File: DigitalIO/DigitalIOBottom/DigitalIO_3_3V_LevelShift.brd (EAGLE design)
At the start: 64 x 82 mm, 72 parts, among them IC1 MCP23017SP, IC2 ULN2803A, K5 HF46105, K6 HF46105, K7 HF46105, K8 HF46105, P1 DF11-06-2DSA, Q1 BS170, Q2 BS170, Q5 691131710002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

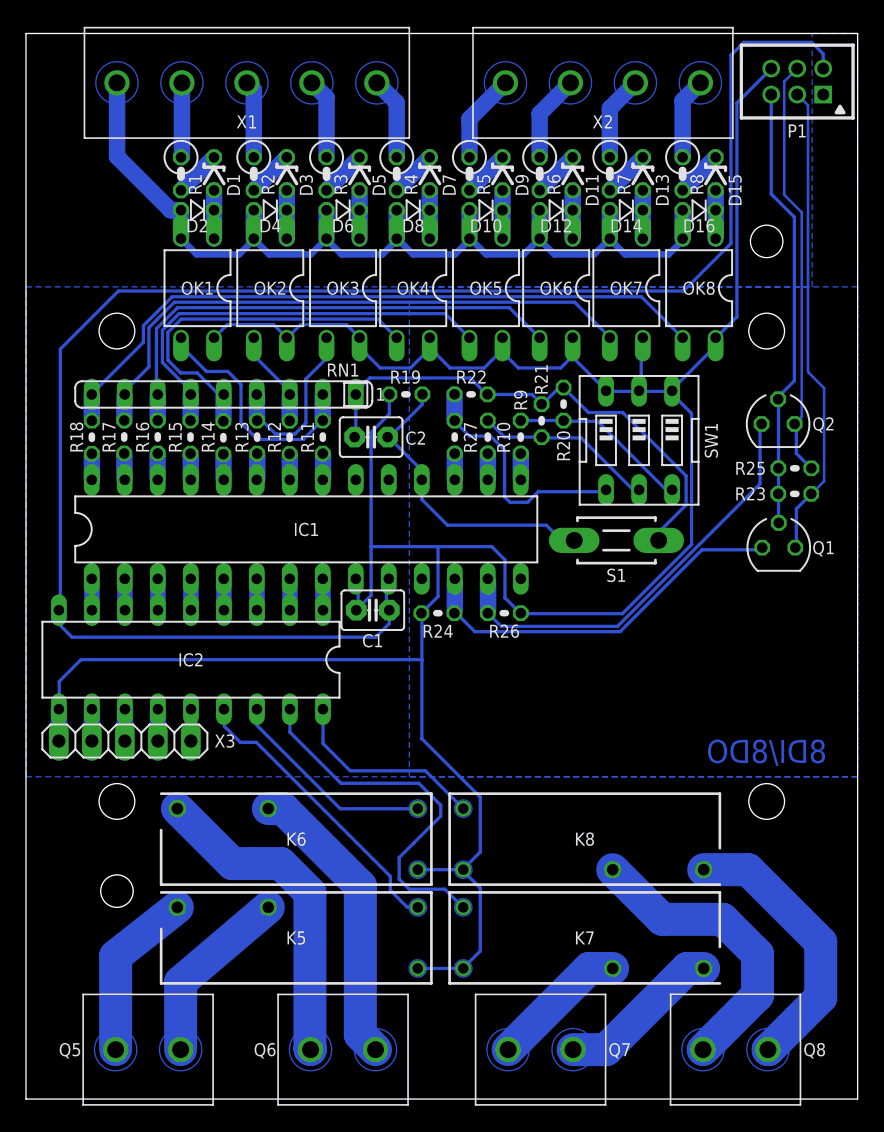
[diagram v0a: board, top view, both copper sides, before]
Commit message: Changed some drills, pads, holes, routes and headers.
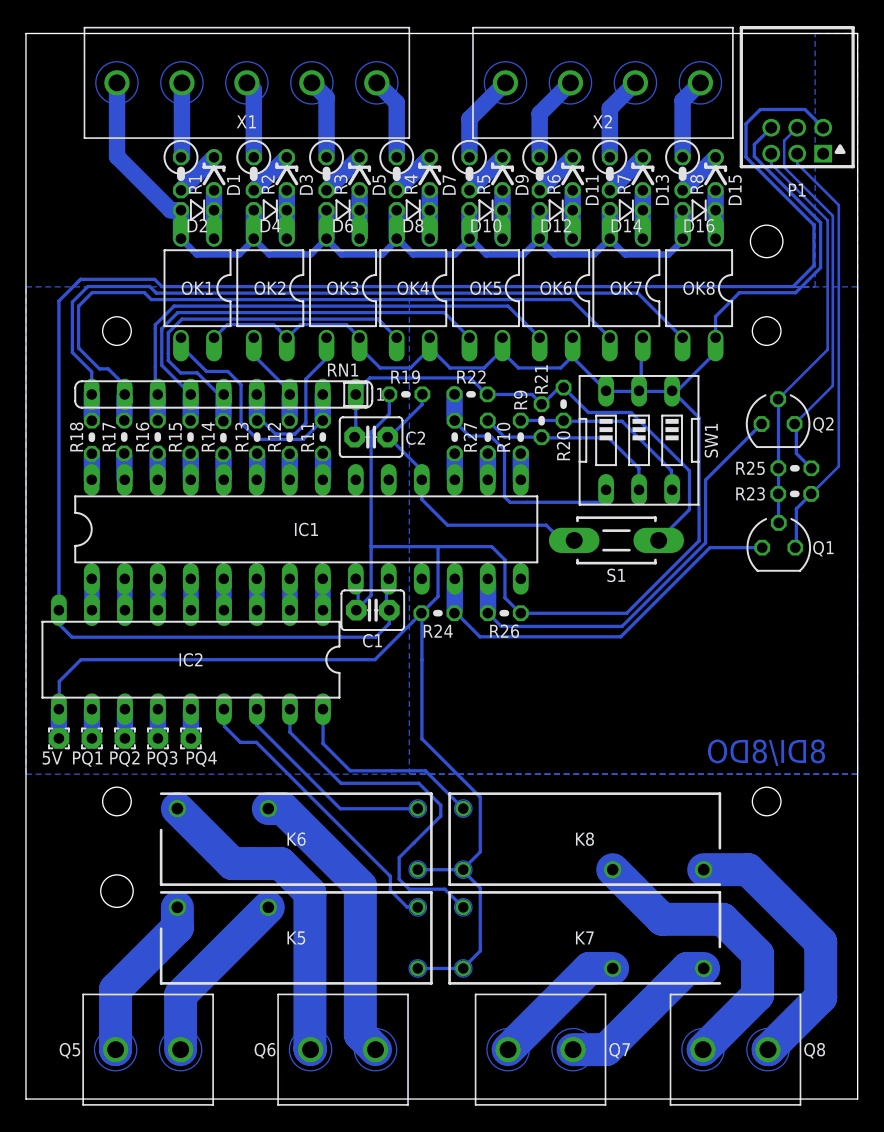
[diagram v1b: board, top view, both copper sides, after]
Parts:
- removed X3: (no value), pinhead:1X05
- added 5V, PQ1, PQ2, PQ3, PQ4: WIREPAD1,6/0,8, wirepad:1,6/0,8
- P1: value DF11-06-2DSA -> DF11-06-2DS; device con-hirose-df11:DF11-06DP-2DSA -> con-hirose-df11:DF11-06DP-2DS
- moved P1 4.55 mm to (59.4, 73.8)
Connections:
- net +5V: now also 5V.1; no longer X3.1
- net N$28: now also PQ4.1; no longer X3.5
- net N$30: now also PQ3.1; no longer X3.4
- net N$32: now also PQ2.1; no longer X3.3
- net N$34: now also PQ1.1; no longer X3.2
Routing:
- net N$49: track 45.3 -> 53.6 mm
- net N$55: track 52.8 -> 59.0 mm
- net GND: track 170.5 -> 176.7 mm
- net +5V: track 222.7 -> 227.0 mm
- net N$71: track 36.6 -> 33.0 mm
- net N$69: track 32.5 -> 30.0 mm
- net +3V3: track 34.2 -> 31.8 mm
- net N$78: track 13.8 -> 14.8 mm
- net N$77: track 13.9 -> 14.7 mm
- net N$34: track 3.03 -> 2.25 mm
- net N$32: track 3.03 -> 2.25 mm
- net N$30: track 3.03 -> 2.25 mm
- net N$28: track 3.03 -> 2.25 mm
- net N$43: track 39.1 -> 38.6 mm

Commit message: Prepare for production.
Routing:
- net N$31: track 29.9 -> 29.3 mm
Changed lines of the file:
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@@
 <wire x1="15.2" y1="54.175" x2="15.22" y2="54.22" width="0.508" layer="16"/>
 <wire x1="28.53" y1="58.57" x2="28.28" y2="58.68" width="0.254" layer="16"/>
-<wire x1="27.08" y1="60.02" x2="27.47" y2="59.63" width="0.254" layer="16"/>
 <wire x1="27.47" y1="59.63" x2="28.53" y2="58.57" width="0.254" layer="16"/>
 <wire x1="13.18" y1="55.88" x2="11.9" y2="55.88" width="0.254" layer="16"/>
@@
 <wire x1="14.62" y1="54.44" x2="15.22" y2="54.22" width="0.254" layer="16"/>
 <wire x1="11.9" y1="55.88" x2="10.95" y2="56.83" width="0.254" layer="16"/>
-<wire x1="10.95" y1="56.83" x2="10.95" y2="57.36" width="0.254" layer="16"/>
-<wire x1="10.95" y1="57.36" x2="10.95" y2="58.96" width="0.254" layer="16"/>
+<wire x1="10.95" y1="56.83" x2="10.95" y2="58.96" width="0.254" layer="16"/>
 <wire x1="10.95" y1="58.96" x2="12.01" y2="60.02" width="0.254" layer="16"/>
 <wire x1="12.01" y1="60.02" x2="27.08" y2="60.02" width="0.254" layer="16"/>
@@
 <wire x1="12.44" y1="54.74" x2="12.17" y2="54.74" width="0.254" layer="16"/>
 <wire x1="12.17" y1="54.74" x2="10.45" y2="56.46" width="0.254" layer="16"/>
-<wire x1="10.45" y1="56.46" x2="10.45" y2="59.13" width="0.254" layer="16"/>
-<wire x1="10.45" y1="59.13" x2="10.45" y2="59.29" width="0.254" layer="16"/>
+<wire x1="10.45" y1="56.46" x2="10.45" y2="59.29" width="0.254" layer="16"/>
 <wire x1="10.45" y1="59.29" x2="11.68" y2="60.52" width="0.254" layer="16"/>
 <wire x1="11.68" y1="60.52" x2="32.2" y2="60.52" width="0.254" layer="16"/>
@@
 <wire x1="10.04" y1="54.74" x2="10.14" y2="54.22" width="0.254" layer="16"/>
 <wire x1="10.04" y1="54.74" x2="9.95" y2="54.83" width="0.254" layer="16"/>
-<wire x1="9.95" y1="54.83" x2="9.95" y2="56.33" width="0.254" layer="16"/>
-<wire x1="9.95" y1="56.33" x2="9.95" y2="59.28" width="0.254" layer="16"/>
-<wire x1="9.95" y1="59.28" x2="9.95" y2="59.57" width="0.254" layer="16"/>
+<wire x1="9.95" y1="54.83" x2="9.95" y2="59.57" width="0.254" layer="16"/>
 <wire x1="9.95" y1="59.57" x2="11.4" y2="61.02" width="0.254" layer="16"/>
 <wire x1="11.4" y1="61.02" x2="37.1" y2="61.02" width="0.254" layer="16"/>
@@
 </polygon>
 <wire x1="31.92" y1="22.61" x2="31.92" y2="21.78" width="0.254" layer="16"/>
-<wire x1="31.92" y1="21.78" x2="29.86" y2="19.72" width="0.254" layer="16"/>
-<wire x1="29.86" y1="19.72" x2="28.72" y2="18.58" width="0.254" layer="16"/>
+<wire x1="31.92" y1="21.78" x2="28.72" y2="18.58" width="0.254" layer="16"/>
 <wire x1="28.72" y1="18.58" x2="28.72" y2="16.92" width="0.254" layer="16"/>
 <wire x1="28.72" y1="16.92" x2="29.49" y2="16.15" width="0.254" layer="16"/>
@@
 </polygon>
 <wire x1="33.65" y1="22.35" x2="30.74" y2="25.26" width="0.254" layer="16"/>
-<wire x1="30.74" y1="25.26" x2="28.11" y2="25.26" width="0.254" layer="16"/>
-<wire x1="28.11" y1="25.26" x2="24.95" y2="25.26" width="0.254" layer="16"/>
+<wire x1="30.74" y1="25.26" x2="24.95" y2="25.26" width="0.254" layer="16"/>
 <wire x1="24.95" y1="25.26" x2="22.86" y2="27.35" width="0.254" layer="16"/>
 <wire x1="22.86" y1="27.35" x2="22.86" y2="29.994884375" width="0.254" layer="16"/>
@@
 </polygon>
 <wire x1="11.65" y1="22.35" x2="15.88" y2="18.12" width="2.54" layer="16"/>
-<wire x1="15.88" y1="18.12" x2="17.48" y2="18.12" width="2.54" layer="16"/>
-<wire x1="17.48" y1="18.12" x2="19.61" y2="18.12" width="2.54" layer="16"/>
+<wire x1="15.88" y1="18.12" x2="19.61" y2="18.12" width="2.54" layer="16"/>
 <wire x1="19.61" y1="18.12" x2="21.85" y2="15.88" width="2.54" layer="16"/>
 <wire x1="21.85" y1="15.88" x2="21.85" y2="3.85" width="2.54" layer="16"/>
@@
 <contactref element="K8" pad="NO"/>
 <contactref element="Q8" pad="1"/>
-<wire x1="61.12" y1="7.79" x2="57.13" y2="3.8" width="2.54" layer="16"/>
+<wire x1="61.16" y1="7.83" x2="57.13" y2="3.8" width="2.54" layer="16"/>
 <wire x1="57.13" y1="3.8" x2="57.1" y2="3.8" width="2.54" layer="16"/>
 <polygon width="0.35" layer="16" thermals="no">
@@
 <wire x1="55.57" y1="17.65" x2="61.16" y2="12.06" width="2.54" layer="16"/>
 <wire x1="61.16" y1="12.06" x2="61.16" y2="7.83" width="2.54" layer="16"/>
-<wire x1="61.16" y1="7.83" x2="61.12" y2="7.79" width="2.54" layer="16"/>
 </signal>
 <signal name="N$40">
@@
 <wire x1="41.36" y1="54.74" x2="41.37" y2="54.75" width="0.254" layer="16"/>
 <wire x1="39.8" y1="53.52" x2="39.68" y2="53.47" width="0.254" layer="16"/>
-<wire x1="43.2816" y1="52.832" x2="45.9232" y2="52.832" width="0.254" layer="16"/>
+<wire x1="43.2816" y1="52.832" x2="46.568" y2="52.832" width="0.254" layer="16"/>
 <wire x1="41.4528" y1="54.6608" x2="43.2816" y2="52.832" width="0.254" layer="16"/>
 <wire x1="41.4528" y1="54.6608" x2="41.37" y2="54.75" width="0.254" layer="16"/>
@@
 <wire x1="61.35" y1="74.75" x2="59.95" y2="76.15" width="0.254" layer="16"/>
 <wire x1="59.95" y1="76.15" x2="56.51" y2="76.15" width="0.254" layer="16"/>
-<wire x1="4.2" y1="63.08" x2="3.935" y2="62.815" width="0.254" layer="16"/>
 <wire x1="3.935" y1="62.815" x2="2.534884375" y2="61.414884375" width="0.254" layer="16"/>
 <wire x1="2.534884375" y1="61.414884375" x2="2.534884375" y2="37.62" width="0.254" layer="16"/>
-<wire x1="51.5" y1="62.52" x2="10.46" y2="62.52" width="0.254" layer="16"/>
+<wire x1="59.03" y1="62.52" x2="10.46" y2="62.52" width="0.254" layer="16"/>
 <wire x1="10.46" y1="62.52" x2="9.9" y2="63.08" width="0.254" layer="16"/>
 <wire x1="9.9" y1="63.08" x2="4.2" y2="63.08" width="0.254" layer="16"/>
@@
 <wire x1="60.64" y1="67.25" x2="60.64" y2="64.13" width="0.254" layer="16"/>
 <wire x1="60.64" y1="64.13" x2="59.03" y2="62.52" width="0.254" layer="16"/>
-<wire x1="59.03" y1="62.52" x2="51.5" y2="62.52" width="0.254" layer="16"/>
-<wire x1="45.9232" y1="52.832" x2="46.568" y2="52.832" width="0.254" layer="16"/>
 <wire x1="46.568" y1="52.832" x2="51.06" y2="48.34" width="0.254" layer="16"/>
 <wire x1="51.06" y1="48.34" x2="51.06" y2="45.36" width="0.254" layer="16"/>
@@
 <wire x1="61.15" y1="67.44" x2="61.15" y2="63.97" width="0.254" layer="16"/>
 <wire x1="53.09" y1="58.61" x2="53.07" y2="58.59" width="0.254" layer="16"/>
-<wire x1="49.73" y1="54.5" x2="49.72" y2="54.5" width="0.254" layer="16"/>
 <wire x1="38.14" y1="37.35" x2="38.17" y2="37.38" width="0.254" layer="16"/>
 <wire x1="38.17" y1="37.38" x2="46.22" y2="37.38" width="0.254" layer="16"/>
@@
 <wire x1="38.08" y1="52.22" x2="38.07" y2="52.21" width="0.254" layer="16"/>
 <wire x1="41.36" y1="52.22" x2="41.37" y2="52.21" width="0.254" layer="16"/>
-<wire x1="41.48" y1="52.16" x2="43.98" y2="52.16" width="0.254" layer="16"/>
+<wire x1="41.48" y1="52.16" x2="45.87" y2="52.16" width="0.254" layer="16"/>
 <wire x1="41.48" y1="52.16" x2="41.37" y2="52.21" width="0.254" layer="16"/>
-<wire x1="43.98" y1="52.16" x2="45.87" y2="52.16" width="0.254" layer="16"/>
 <wire x1="45.87" y1="52.16" x2="49.67" y2="48.36" width="0.254" layer="16"/>
 <wire x1="49.67" y1="48.36" x2="49.67" y2="46.93" width="0.254" layer="16"/>
@@
 <wire x1="35.54" y1="52.2" x2="35.54" y2="52.21" width="0.254" layer="16"/>
 <wire x1="39.68" y1="50.94" x2="39.68" y2="50.93" width="0.254" layer="16"/>
-<wire x1="39.8" y1="50.88" x2="42.72" y2="50.88" width="0.254" layer="16"/>
+<wire x1="39.8" y1="50.88" x2="44.83" y2="50.88" width="0.254" layer="16"/>
 <wire x1="39.8" y1="50.88" x2="39.68" y2="50.93" width="0.254" layer="16"/>
-<wire x1="42.72" y1="50.88" x2="44.83" y2="50.88" width="0.254" layer="16"/>
 <wire x1="44.83" y1="50.88" x2="47.17" y2="48.54" width="0.254" layer="16"/>
 <wire x1="47.17" y1="48.54" x2="47.17" y2="46.89" width="0.254" layer="16"/>
@@
 <wire x1="32.98" y1="54.23" x2="32.98" y2="52.22" width="1.27" layer="16"/>
 <wire x1="32.98" y1="52.22" x2="32.99" y2="52.21" width="0.254" layer="16"/>
-<wire x1="37.242" y1="45.9232" x2="38.608" y2="45.9232" width="0.254" layer="16"/>
 <wire x1="36.826" y1="46.3392" x2="37.242" y2="45.9232" width="0.254" layer="16"/>
 <wire x1="36.826" y1="49.9404" x2="36.826" y2="46.3392" width="0.254" layer="16"/>
@@
 <wire x1="33.1216" y1="52.0192" x2="34.1244" y2="51.0164" width="0.254" layer="16"/>
 <wire x1="33.1216" y1="52.0192" x2="32.99" y2="52.21" width="0.254" layer="16"/>
-<wire x1="38.608" y1="45.9232" x2="44.2532" y2="45.9232" width="0.254" layer="16"/>
+<wire x1="37.242" y1="45.9232" x2="44.2532" y2="45.9232" width="0.254" layer="16"/>
 <wire x1="44.2532" y1="45.9232" x2="44.64" y2="46.31" width="0.254" layer="16"/>
 <wire x1="44.64" y1="46.31" x2="44.64" y2="46.88" width="0.254" layer="16"/>
